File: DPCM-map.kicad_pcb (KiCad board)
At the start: 2 copper layers, 180 x 180 mm, 1 part

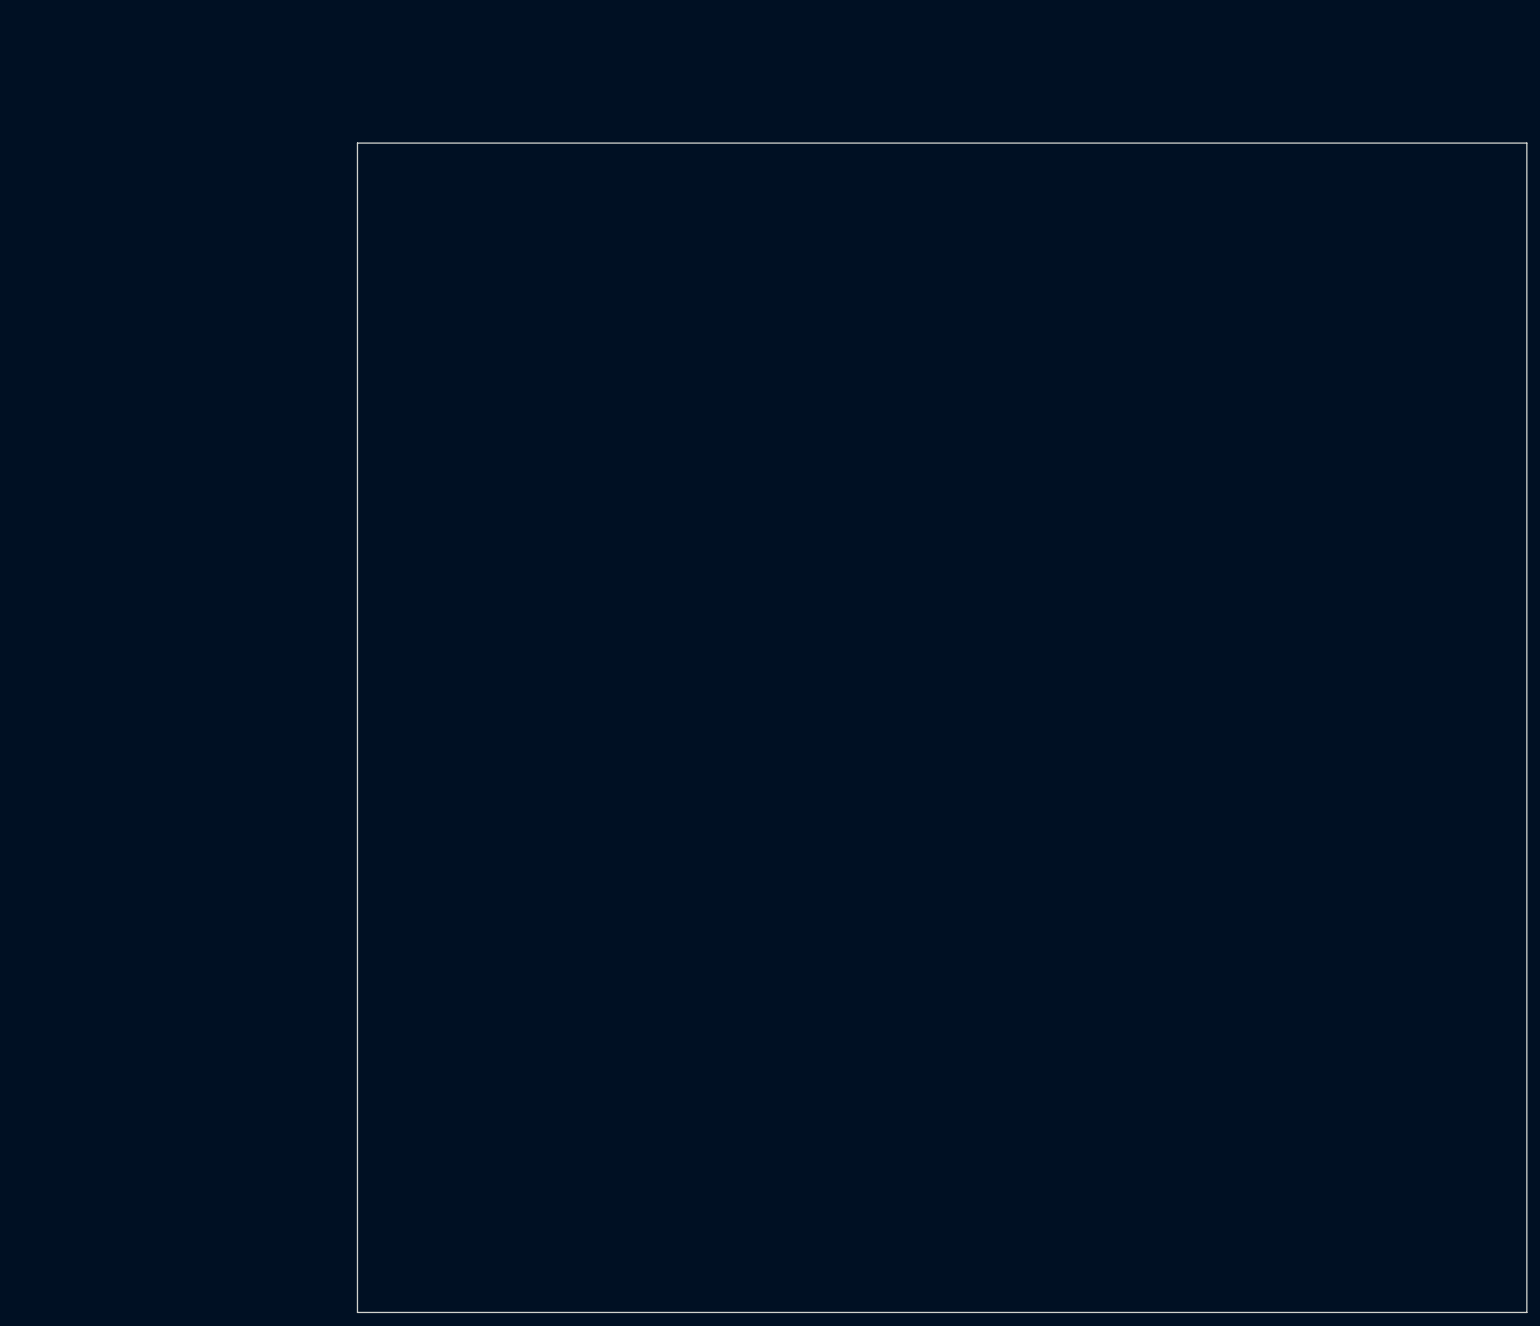
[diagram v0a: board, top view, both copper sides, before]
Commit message: added rounded edges to pcb
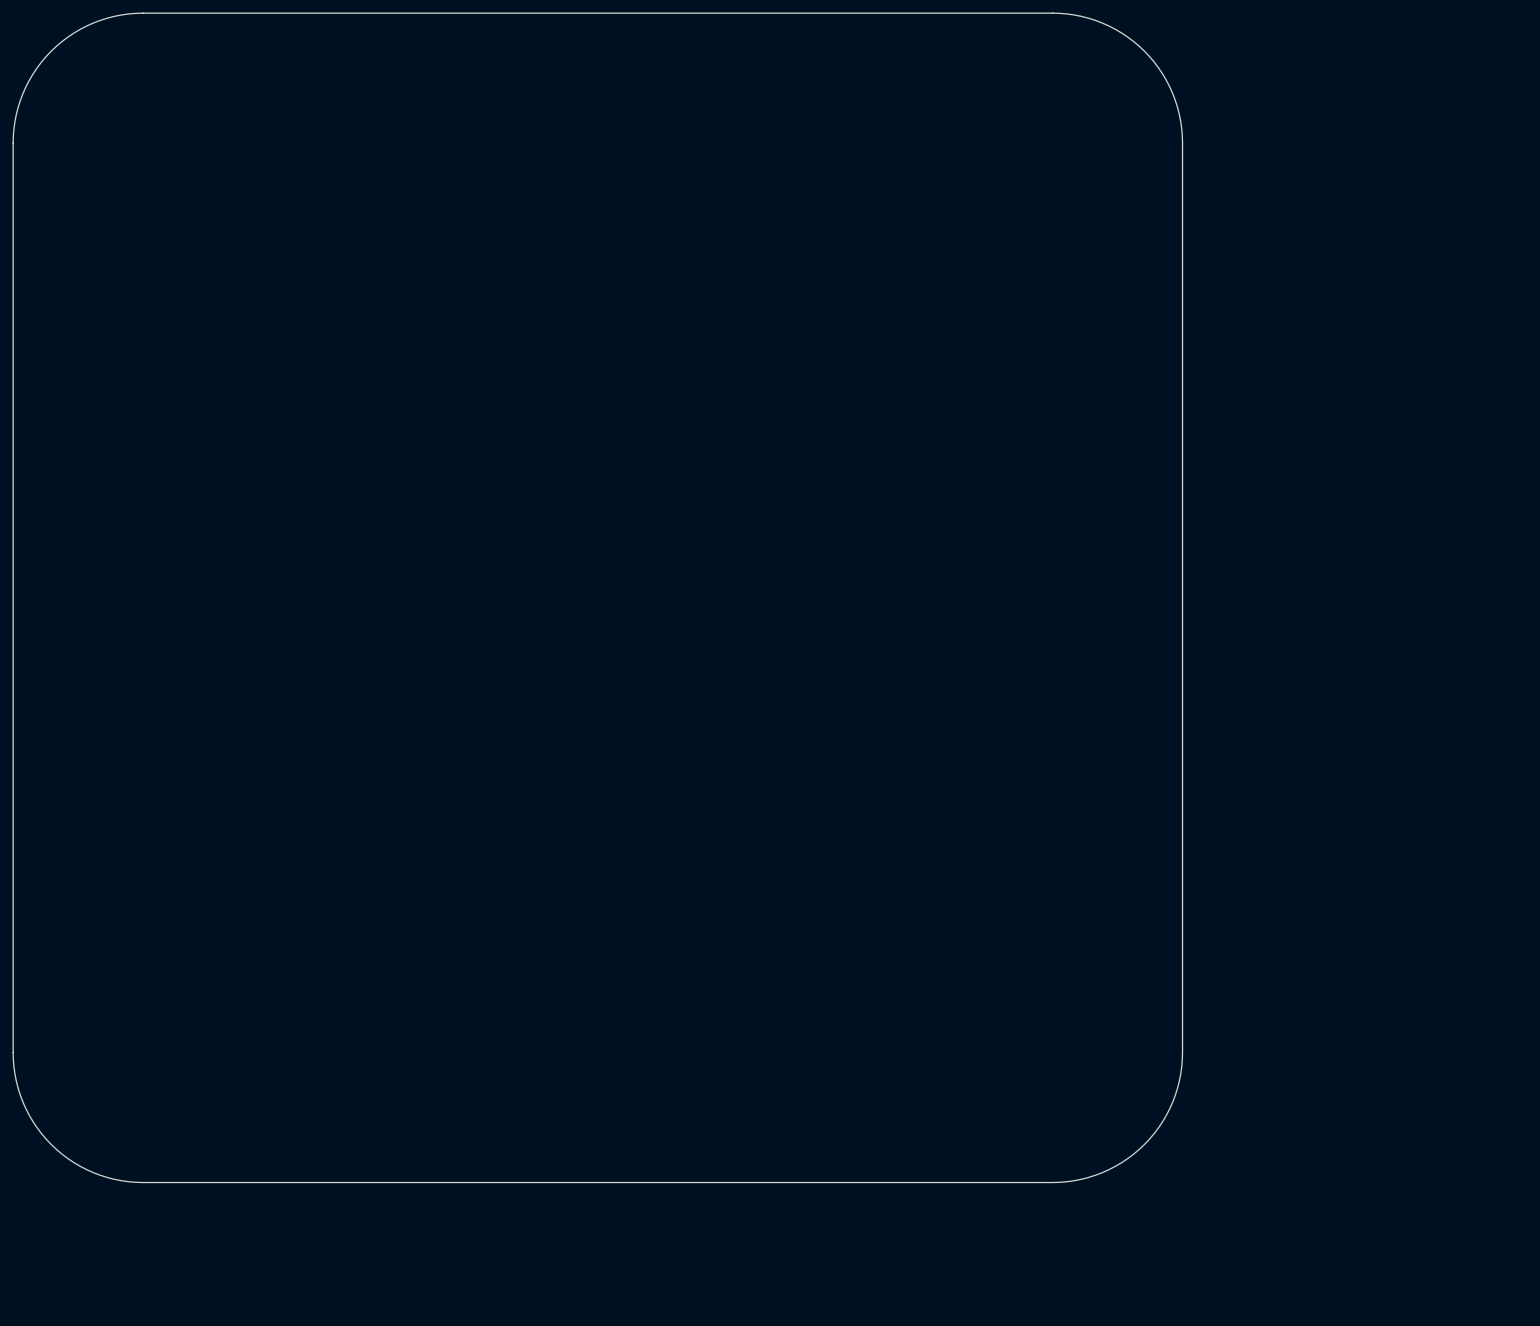
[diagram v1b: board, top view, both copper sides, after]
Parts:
- moved G*** 56.6 mm to (180.0, 180.0)
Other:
- outline, holes or cut-outs redrawn
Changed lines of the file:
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@@
   (general
     (thickness 1.6)
-    (drawings 4)
+    (drawings 8)
     (tracks 0)
     (zones 0)
@@
     (solder_mask_min_width 0.25)
     (aux_axis_origin 0 0)
-    (visible_elements FFFFFF7F)
+    (visible_elements 7FFFFFFF)
     (pcbplotparams
       (layerselection 0x010fc_ffffffff)
@@
   )
   (module mapref:mapref (layer F.Cu)
-    (at 233 200)
+    (at 180 180)
     (fp_text reference G*** (at -90.09 -90.09) (layer F.SilkS) hide
       (effects (font (size 1.524 1.524) (thickness 0.3)))
@@
       (xy -0.004666 -180.090745) (xy -0.004666 -0.004666)) (layer Eco2.User) (width 0.01))
   )
-  (gr_line (start 233 20) (end 233 200) (layer Edge.Cuts) (width 0.05))
-  (gr_line (start 53 20) (end 53 200) (layer Edge.Cuts) (width 0.05))
-  (gr_line (start 53 200) (end 233 200) (layer Edge.Cuts) (width 0.05))
-  (gr_line (start 53 20) (end 233 20) (layer Edge.Cuts) (width 0.05))
+  (gr_line (start 160 0) (end 20 0) (layer Edge.Cuts) (width 0.05))
+  (gr_arc (start 160 20) (end 180 20) (angle -90) (layer Edge.Cuts) (width 0.05))
+  (gr_line (start 180 160) (end 180 20) (layer Edge.Cuts) (width 0.05))
+  (gr_arc (start 160 160) (end 160 180) (angle -90) (layer Edge.Cuts) (width 0.05))
+  (gr_line (start 20 180) (end 160 180) (layer Edge.Cuts) (width 0.05))
+  (gr_arc (start 20 160) (end 0 160) (angle -90) (layer Edge.Cuts) (width 0.05))
+  (gr_line (start 0 20) (end 0 160) (layer Edge.Cuts) (width 0.05))
+  (gr_arc (start 20 20) (end 20 0) (angle -90) (layer Edge.Cuts) (width 0.05))
 )
